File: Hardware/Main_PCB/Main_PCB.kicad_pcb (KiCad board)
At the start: 4 copper layers, 65 x 49 mm, 89 parts, among them J201 Sonar, J301 2171790001, J601 Conn_01x08_Pin, J602 Conn_01x03_Pin, J603 Servo con, SW301 TL3342F160QG_TR, SW302 TL3342F160QG_TR, U201 TUSS4470TRTJT, U301 RP2040, U302 W25Q128JVS, U401 TPS62170DSG, U402 TPS61175PWPR, U403 BD50FD0WFP2-E2, U501 ICM-42688-P, U601 NRF24L01, U602 SN74LV1T34DBV, Y301 12MHz

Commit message: Should be finished version of MainPCB - v2
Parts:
- moved C208 5.90 mm to (116.4, 64.2)
- moved R403 4.75 mm to (102.0, 82.7), turned to 180 degrees
- moved C406 3.81 mm to (105.7, 83.8)
- moved C408 2.18 mm to (105.7, 88.7), turned to 180 degrees
- moved R404 1.58 mm to (101.5, 87.4)
- moved C206 1.46 mm to (116.4, 65.8), turned to 0 degrees
- moved C407 1.32 mm to (105.7, 86.2), turned to 180 degrees
- moved L401 1.31 mm to (97.2, 75.1)
- moved C402 1.27 mm to (97.7, 71.2)
- moved R407 1.20 mm to (107.2, 81.9)
- moved D201 0.56 mm to (107.7, 70.1)
- moved D401 0.45 mm to (103.9, 73.3)
- moved L402 0.09 mm to (101.8, 85.0), turned to 0 degrees
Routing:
- net +3.3V: track 65.6 -> 81.2 mm, vias 12 -> 15
- net +12V: track 2.62 -> 12.0 mm, vias 1 -> 5
- net +5V: track 12.0 -> 3.12 mm, vias 4 -> 6
- net Net-(U402-FREQ): track 0.00 -> 6.29 mm
- net Net-(U402-FB): track 0.00 -> 5.62 mm
- net Net-(U402-SS): track 0.00 -> 3.16 mm
- net Net-(U401-FB): track 0.00 -> 3.12 mm
- net Net-(C406-Pad1): track 0.00 -> 2.37 mm
- net Net-(U201-VDRV): track 45.9 -> 43.7 mm
- net Net-(U402-COMP): track 0.00 -> 1.92 mm
- net Net-(U401-SW): track 0.00 -> 1.89 mm
- net VDC: track 10.8 -> 9.12 mm, vias 1 -> 5
- net GND: track 43.1 -> 44.8 mm, vias 62 -> 78
- net Net-(J301-CC2): track 3.82 -> 4.57 mm
- net /RP2040/GPIO5: track 87.1 -> 86.4 mm
- added copper zone on F.Cu, net +12V
- added copper zone on F.Cu, net +3.3V
- added copper zone on F.Cu, net +5V
- added copper zone on F.Cu, net Net-(D401-A)
- added copper zone on F.Cu, net VDC

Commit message: Finished MainPCB v3
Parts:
- added TP601: +VPROT test point, TestPoint:TestPoint_Pad_D1.0mm, F.Cu at (93.8, 95.2)
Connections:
- net VDC renamed +VPROT
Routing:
- net Net-(U401-SW): track 1.89 -> 0.04 mm
- added copper zone on F.Cu, net Net-(U401-SW)
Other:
- board text added: "+VPROT"
- board text added: "12V"
- board text added: "3.3V"
- board text added: "5V"
- board text added: "Main PCB Group 6 ESPRO3"

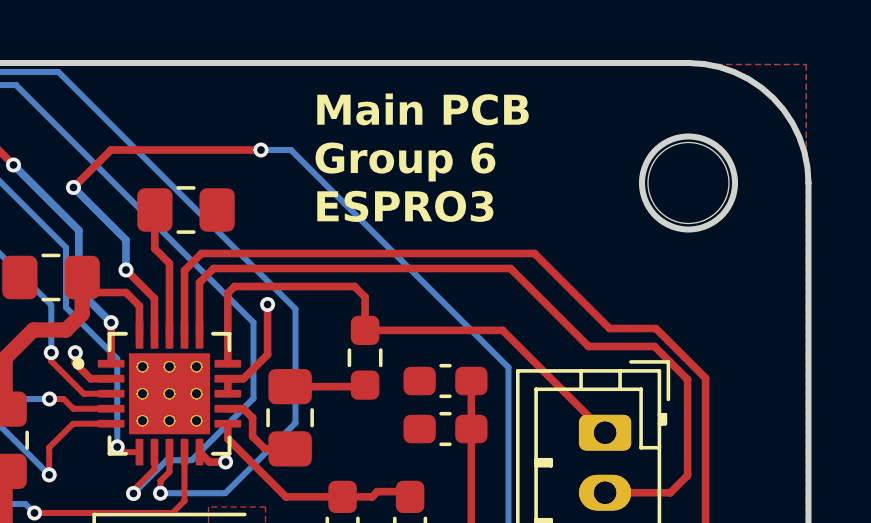
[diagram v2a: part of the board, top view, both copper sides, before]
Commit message: Small adjustment to top silkscreen on MainPCB
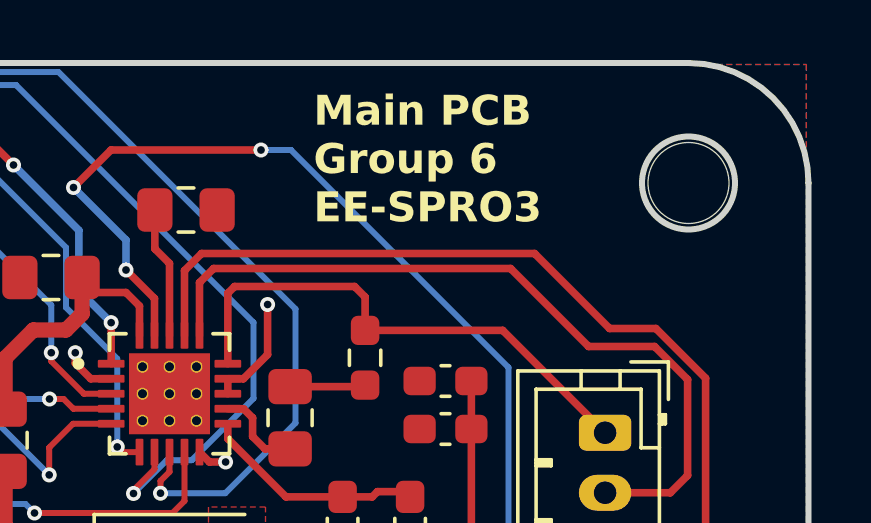
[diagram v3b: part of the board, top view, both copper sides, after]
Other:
- board text added: "Main PCB Group 6 EE-SPRO3"
- board text removed: "Main PCB Group 6 ESPRO3"
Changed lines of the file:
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@@
 		)
 	)
-	(gr_text "Main PCB\nGroup 6\nESPRO3"
+	(gr_text "Main PCB\nGroup 6\nEE-SPRO3"
 		(at 112 59 0)
 		(layer "F.SilkS")

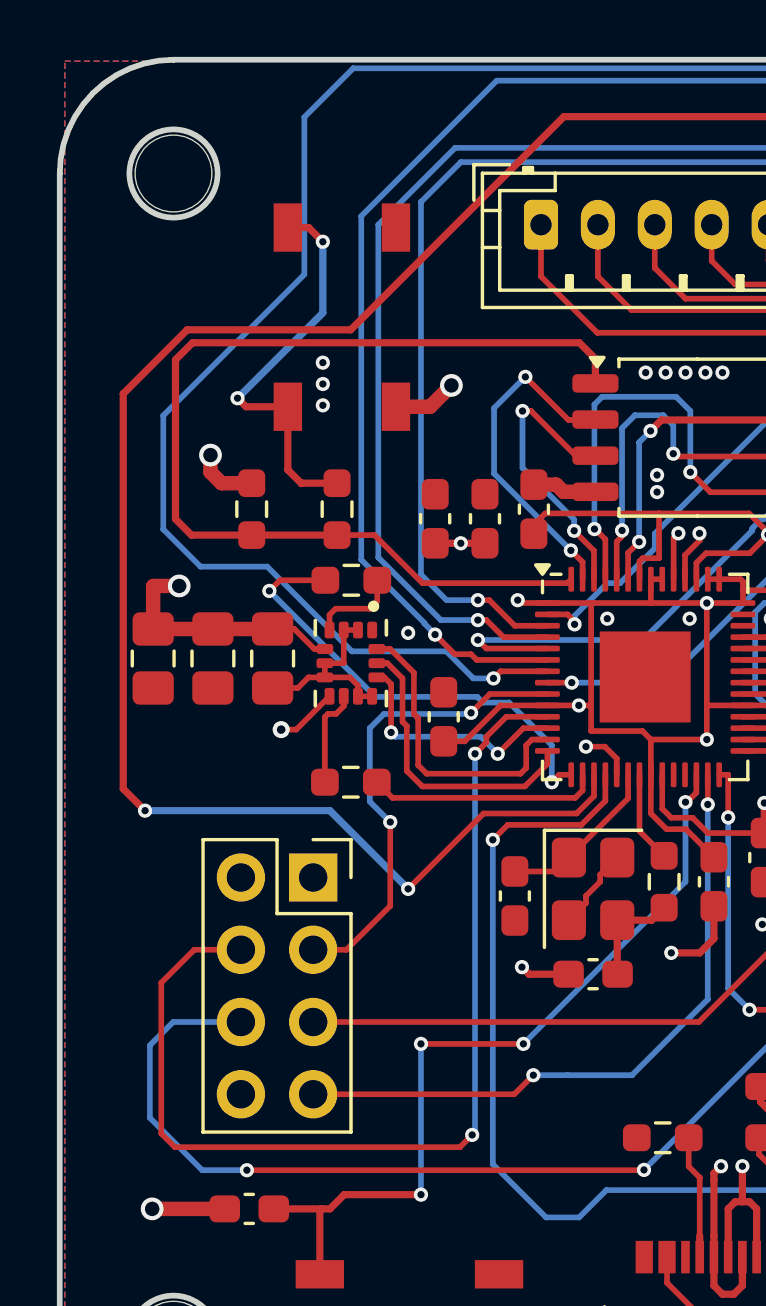
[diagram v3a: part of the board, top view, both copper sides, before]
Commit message: Changed the IMU sensor on the MainPCB
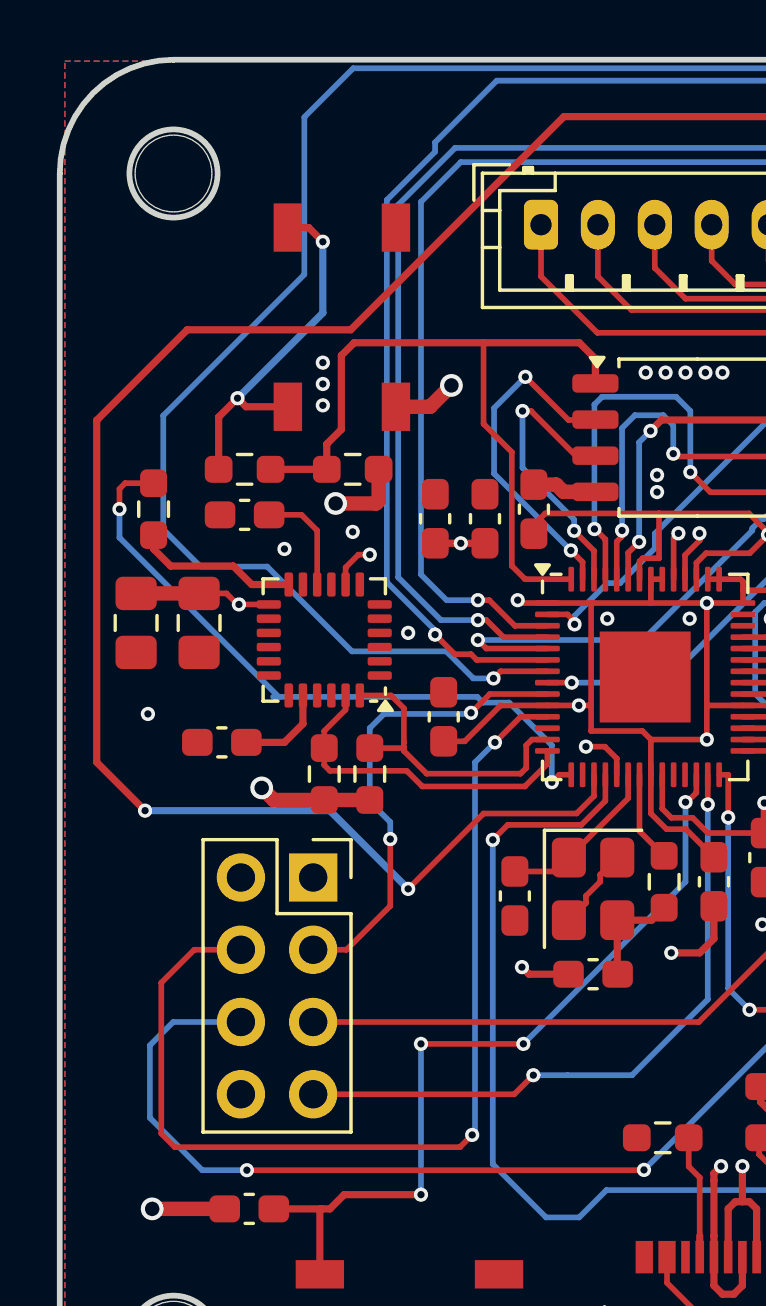
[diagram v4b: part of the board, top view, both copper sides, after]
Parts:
- removed the C502 at (68.9, 74.7)
- added C503: 100n, Capacitor_SMD:C_0603_1608Metric_Pad1.08x0.95mm_HandSolder, F.Cu at (70.0, 69.6)
- added C504: 2.2n, Capacitor_SMD:C_0603_1608Metric_Pad1.08x0.95mm_HandSolder, F.Cu at (69.2, 77.6)
- added R503: 100, Resistor_SMD:R_0603_1608Metric_Pad0.98x0.95mm_HandSolder, F.Cu at (66.8, 69.4)
- R501, R502: value 100 -> 5.1k
- U501: value ICM-42688-P -> MPU-6050; footprint MainPCB:PQFN50P300X250X97-14N -> Sensor_Motion:InvenSense_QFN-24_4x4mm_P0.5mm
- moved R502 6.88 mm to (72.8, 78.7), turned to -90 degrees
- moved R308 3.82 mm to (73.8, 68.0), turned to 180 degrees
- moved R307 3.54 mm to (70.0, 68.0), turned to 180 degrees
- moved C501 2.87 mm to (68.4, 73.4), turned to 90 degrees
- moved C502 1.39 mm to (66.2, 73.4)
- moved U501 1.24 mm to (72.8, 74.0), turned to 180 degrees
- moved R501 0.72 mm to (74.4, 78.7), turned to -90 degrees
- renumbered C503 to C502
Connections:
- C501 pad 1: +3.3V -> GND
- C501 pad 2: GND -> +3.3V
- R501 pad 1: /ICM42688/INT2 -> /ICM42688/AP_SDA
- R501 pad 2: Net-(U501-INT2/FSYNC/CLKIN) -> +3.3V
- R502 pad 1: Net-(U501-INT1/INT) -> /ICM42688/AP_SCL
- R502 pad 2: /ICM42688/INT1 -> +3.3V
- U301 pad 12: /ICM42688/AP_CS -> /RP2040/GPIO9
- U301 pad 16: /ICM42688/INT2 -> /RP2040/GPIO13
- U501 pad 10: GND -> Net-(U501-REGOUT)
- U501 pad 12: /ICM42688/AP_CS -> Net-(U501-INT)
- U501 pad 13: /ICM42688/AP_SCL -> +3.3V
- U501 pad 14: /ICM42688/AP_SDA -> unconnected-(U501-NC-Pad14)
- U501 pad 2: GND -> unconnected-(U501-NC-Pad2)
- U501 pad 3: GND -> unconnected-(U501-NC-Pad3)
- U501 pad 4: Net-(U501-INT1/INT) -> unconnected-(U501-NC-Pad4)
- U501 pad 5: +3.3V -> unconnected-(U501-NC-Pad5)
- U501 pad 6: GND -> unconnected-(U501-AUX_DA-Pad6)
- U501 pad 7: GND -> unconnected-(U501-AUX_CL-Pad7)
- U501 pad 9: Net-(U501-INT2/FSYNC/CLKIN) -> GND
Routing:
- net /RP2040/QSPI_SS: track 36.6 -> 27.2 mm
- net /ICM42688/AP_CS: track 8.74 -> 0.00 mm, vias 2 -> 0
- net /ICM42688/INT2: track 8.12 -> 0.00 mm
- net /ICM42688/INT1: track 16.4 -> 23.5 mm
- net GND: track 44.8 -> 37.8 mm, vias 78 -> 81
- net Net-(U501-INT): track 0.00 -> 5.76 mm
- net Net-(U501-REGOUT): track 0.00 -> 3.82 mm
- net Net-(U501-INT2/FSYNC/CLKIN): track 3.46 -> 0.00 mm
- net Net-(U501-CPOUT): track 0.00 -> 3.26 mm
- net Net-(U501-INT1/INT): track 3.15 -> 0.00 mm
- net /RP2040/~{USB_BOOT}: track 14.2 -> 12.8 mm
- net /ICM42688/AP_SCL: track 10.5 -> 11.7 mm
- net /OUT3: track 82.9 -> 83.6 mm
- net /RP2040/GPIO4: track 70.8 -> 70.0 mm
- net /RP2040/GPIO2: track 58.4 -> 57.8 mm
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
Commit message: Minor adjustments to MainPCB
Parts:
- C501: footprint Capacitor_SMD:C_0805_2012Metric_Pad1.18x1.45mm_HandSolder -> Capacitor_SMD:C_0603_1608Metric_Pad1.08x0.95mm_HandSolder
- moved C501 6.67 mm to (74.1, 70.0), turned to 0 degrees
- moved C502 2.22 mm to (68.4, 73.4)
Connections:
- net /ICM42688/AP_SCL renamed /MPU6050/AP_SCL
- net /ICM42688/AP_SDA renamed /MPU6050/AP_SDA
- net /ICM42688/INT1 renamed /MPU6050/INT1
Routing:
- net GND: track 37.8 -> 40.0 mm, vias 81 -> 118
- net +3.3V: track 81.1 -> 82.0 mm, vias 16 -> 15
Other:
- board text added: "JLCJLCJLCJLC"

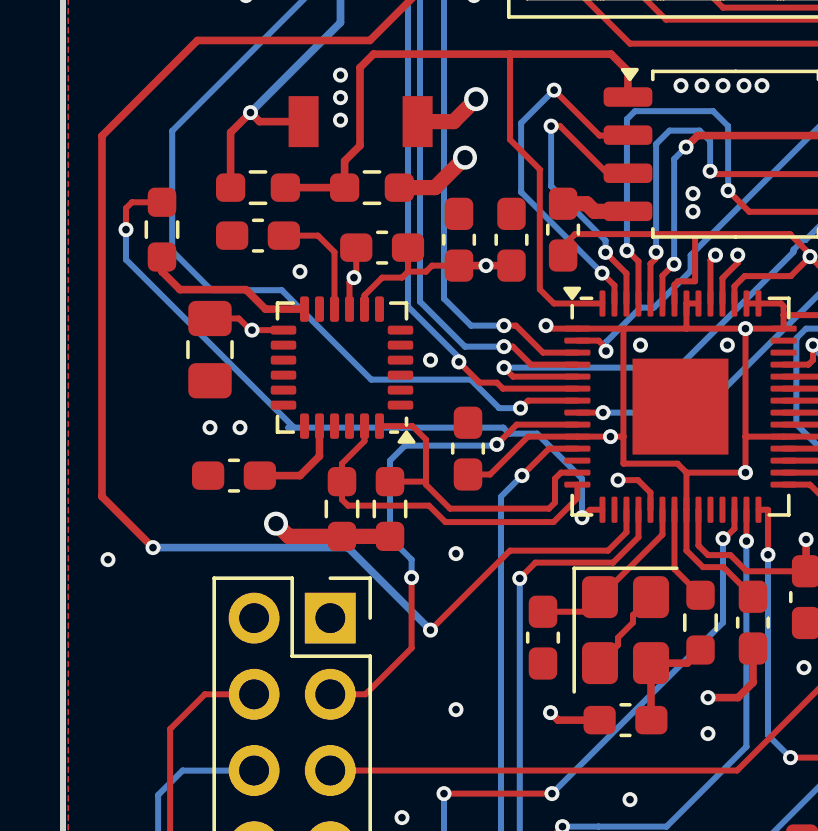
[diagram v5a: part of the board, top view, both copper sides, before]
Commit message: Reverted to the previous IMU
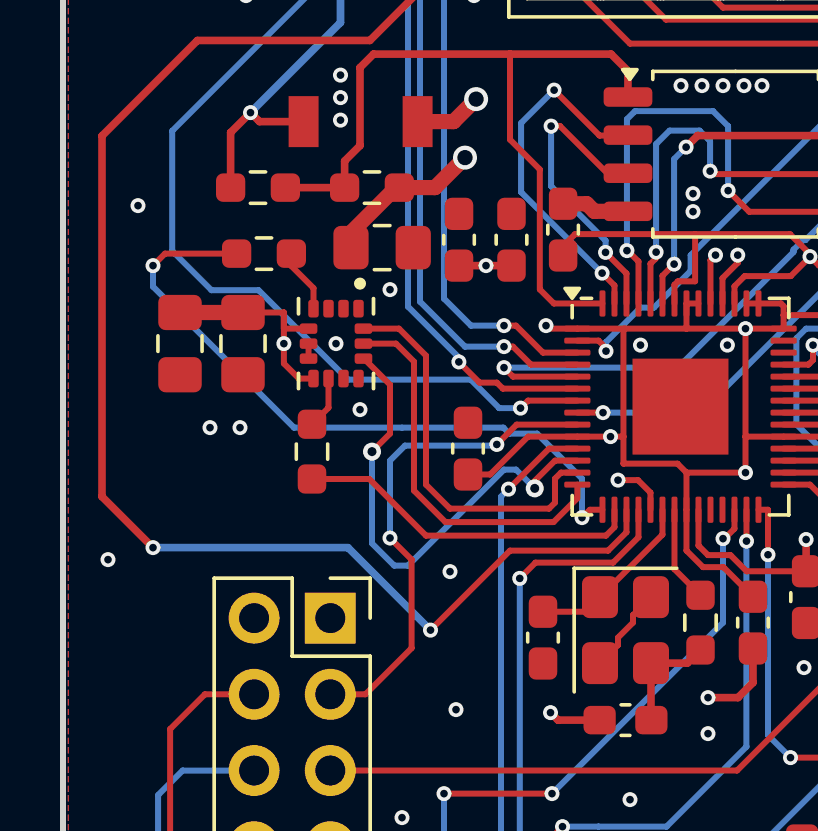
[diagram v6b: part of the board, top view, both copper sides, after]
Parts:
- removed the C503 at (70.0, 69.6)
- removed C504: 2.2n, Capacitor_SMD:C_0603_1608Metric_Pad1.08x0.95mm_HandSolder
- removed R503: 100, Resistor_SMD:R_0603_1608Metric_Pad0.98x0.95mm_HandSolder
- added C502: 2.2u, Capacitor_SMD:C_0805_2012Metric_Pad1.18x1.45mm_HandSolder, F.Cu at (67.4, 73.2)
- C501: footprint Capacitor_SMD:C_0603_1608Metric_Pad1.08x0.95mm_HandSolder -> Capacitor_SMD:C_0805_2012Metric_Pad1.18x1.45mm_HandSolder
- R501, R502: value 5.1k -> 100
- U501: value MPU-6050 -> ICM-42688-P; footprint Sensor_Motion:InvenSense_QFN-24_4x4mm_P0.5mm -> MainPCB:PQFN50P300X250X97-14N
- moved R502 8.90 mm to (70.2, 70.2), turned to 180 degrees
- moved R501 3.23 mm to (71.8, 76.8), turned to 90 degrees
- moved C503 1.12 mm to (69.5, 73.2)
- moved U501 0.82 mm to (72.6, 73.2), turned to -90 degrees
- renumbered C502 to C503
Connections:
- C501 pad 1: GND -> +3.3V
- C501 pad 2: +3.3V -> GND
- R501 pad 1: /MPU6050/AP_SDA -> /MPU6050/INT2
- R501 pad 2: +3.3V -> Net-(U501-INT2/FSYNC/CLKIN)
- R502 pad 1: /MPU6050/AP_SCL -> Net-(U501-INT1/INT)
- R502 pad 2: +3.3V -> /MPU6050/INT1
- U301 pad 12: /RP2040/GPIO9 -> /MPU6050/AP_CS
- U301 pad 16: /RP2040/GPIO13 -> /MPU6050/INT2
- U501 pad 10: Net-(U501-REGOUT) -> GND
- U501 pad 12: Net-(U501-INT) -> /MPU6050/AP_CS
- U501 pad 13: +3.3V -> /MPU6050/AP_SCL
- U501 pad 14: unconnected-(U501-NC-Pad14) -> /MPU6050/AP_SDA
- U501 pad 2: unconnected-(U501-NC-Pad2) -> GND
- U501 pad 3: unconnected-(U501-NC-Pad3) -> GND
- U501 pad 4: unconnected-(U501-NC-Pad4) -> Net-(U501-INT1/INT)
- U501 pad 5: unconnected-(U501-NC-Pad5) -> +3.3V
- U501 pad 6: unconnected-(U501-AUX_DA-Pad6) -> GND
- U501 pad 7: unconnected-(U501-AUX_CL-Pad7) -> GND
- U501 pad 9: GND -> Net-(U501-INT2/FSYNC/CLKIN)
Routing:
- net /MPU6050/AP_CS: track 0.00 -> 16.1 mm, vias 0 -> 2
- net /MPU6050/INT2: track 0.00 -> 11.6 mm
- net Net-(U501-INT): track 5.76 -> 0.00 mm
- net Net-(U501-REGOUT): track 3.82 -> 0.00 mm
- net Net-(U501-CPOUT): track 3.26 -> 0.00 mm
- net /MPU6050/AP_SDA: track 10.8 -> 13.1 mm
- net Net-(U501-INT1/INT): track 0.00 -> 2.14 mm
- net Net-(U501-INT2/FSYNC/CLKIN): track 0.00 -> 1.75 mm
- net GND: track 40.0 -> 38.3 mm, vias 118 -> 119
- net /MPU6050/AP_SCL: track 11.7 -> 12.9 mm
- net +3.3V: track 82.0 -> 81.1 mm, vias 15 -> 14
- net /MPU6050/INT1: track 23.5 -> 22.7 mm

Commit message: Footprint updated
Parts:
- J301: footprint MainPCB:2171790001_MOL -> SPRO3:2171790001_MOL
- R501: value 100 -> 1k
- U201: footprint MainPCB:QFN50P400X400X80-21N -> SPRO3:QFN50P400X400X80-21N
- U402: footprint MainPCB:IC_TPS27S100BPWPR -> SPRO3:IC_TPS27S100BPWPR
- U501: footprint MainPCB:PQFN50P300X250X97-14N -> SPRO3:PQFN50P300X250X97-14N
- moved C501 5.61 mm to (68.9, 72.0), turned to 180 degrees
- moved C503 3.99 mm to (70.9, 76.9)
- moved C502 3.99 mm to (68.8, 76.9)
- moved R501 0.91 mm to (72.7, 76.9)
- moved J301 0.51 mm to (87.2, 98.5)
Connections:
- net /MPU6050/AP_CS renamed /ICM42688 - Gyro/AP_CS
- net /MPU6050/AP_SCL renamed /ICM42688 - Gyro/AP_SCL
- net /MPU6050/AP_SDA renamed /ICM42688 - Gyro/AP_SDA
- net /MPU6050/INT1 renamed /ICM42688 - Gyro/INT1
- R501 pad 1: /MPU6050/INT2 -> GND
- U301 pad 16: /MPU6050/INT2 -> /ICM42688 - Gyro/AP_SDO
- U501 pad 1: GND -> /ICM42688 - Gyro/AP_SDO
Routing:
- net /ICM42688 - Gyro/AP_SDO: track 0.00 -> 15.6 mm, vias 0 -> 2
- net /MPU6050/INT2: track 11.6 -> 0.00 mm
- net +3.3V: track 81.1 -> 78.5 mm, vias 14 -> 15
- net GND: track 38.3 -> 39.5 mm, vias 119 -> 122
